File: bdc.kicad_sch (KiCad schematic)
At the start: 0 parts

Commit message: corrected output/input type of pins
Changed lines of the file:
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@@
 	)
 	(hierarchical_label "9"
-		(shape input)
+		(shape output)
 		(at 215.9 54.61 0)
 		(effects
@@
 	)
 	(hierarchical_label "0"
-		(shape input)
+		(shape output)
 		(at 118.11 31.75 0)
 		(effects
@@
 	)
 	(hierarchical_label "7"
-		(shape input)
+		(shape output)
 		(at 124.46 165.1 0)
 		(effects
@@
 	)
 	(hierarchical_label "8"
-		(shape input)
+		(shape output)
 		(at 215.9 36.83 0)
 		(effects
@@
 	)
 	(hierarchical_label "2"
-		(shape input)
+		(shape output)
 		(at 125.73 69.85 0)
 		(effects
@@
 	)
 	(hierarchical_label "6"
-		(shape input)
+		(shape output)
 		(at 124.46 147.32 0)
 		(effects
@@
 	)
 	(hierarchical_label "4"
-		(shape input)
+		(shape output)
 		(at 124.46 111.76 0)
 		(effects
@@
 	)
 	(hierarchical_label "5"
-		(shape input)
+		(shape output)
 		(at 124.46 129.54 0)
 		(effects
@@
 	)
 	(hierarchical_label "3"
-		(shape input)
+		(shape output)
 		(at 125.73 87.63 0)
 		(effects
@@
 	)
 	(hierarchical_label "1"
-		(shape input)
+		(shape output)
 		(at 125.73 52.07 0)
 		(effects
@@
 			)
 		)
-		(pin "Out" input
+		(pin "Out" output
 			(at 176.53 38.1 0)
 			(effects
@@
 			)
 		)
-		(pin "Out" input
+		(pin "Out" output
 			(at 118.11 111.76 0)
 			(effects
@@
 			)
 		)
-		(pin "Out" input
+		(pin "Out" output
 			(at 86.36 31.75 0)
 			(effects
@@
 			)
 		)
-		(pin "Out" input
+		(pin "Out" output
 			(at 118.11 129.54 0)
 			(effects
@@
 			)
 		)
-		(pin "Out" input
+		(pin "Out" output
 			(at 119.38 69.85 0)
 			(effects
@@
 			)
 		)
-		(pin "Out" input
+		(pin "Out" output
 			(at 119.38 52.07 0)
 			(effects
@@
 			)
 		)
-		(pin "Out" input
+		(pin "Out" output
 			(at 119.38 87.63 0)
 			(effects
@@
 			)
 		)
-		(pin "Out" input
+		(pin "Out" output
 			(at 209.55 54.61 0)
 			(effects
@@
 			)
 		)
-		(pin "Out" input
+		(pin "Out" output
 			(at 209.55 36.83 0)
 			(effects
@@
 			)
 		)
-		(pin "Out" input
+		(pin "Out" output
 			(at 118.11 165.1 0)
 			(effects
@@
 			)
 		)
-		(pin "Out" input
+		(pin "Out" output
 			(at 86.36 57.15 0)
 			(effects
@@
 			)
 		)
-		(pin "Out" input
+		(pin "Out" output
 			(at 118.11 147.32 0)
 			(effects

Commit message: schematic cleanup, routed 1 bdc
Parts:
- added C50, C53, C56: 100n, Capacitor_SMD:C_0603_1608Metric, symbol Device:C
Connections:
- new net +3V3: C50.1, C53.1, C56.1
- new net GND: C50.2, C53.2, C56.2

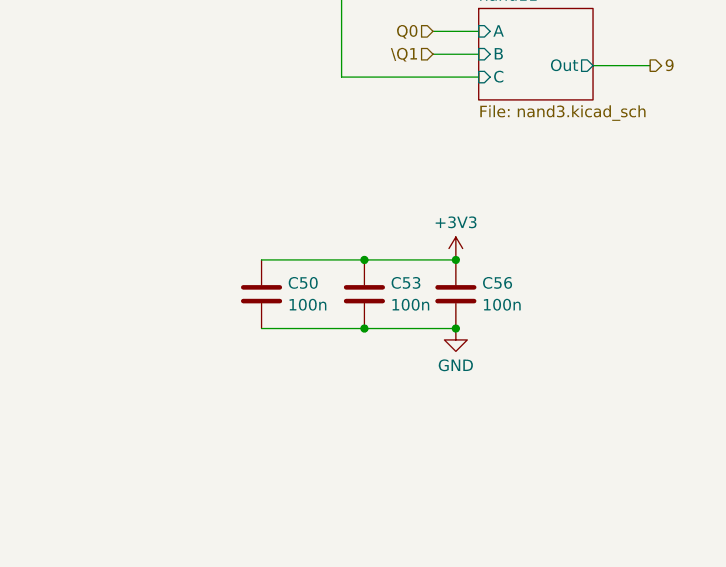
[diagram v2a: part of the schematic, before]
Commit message: started on binary to decimal converter
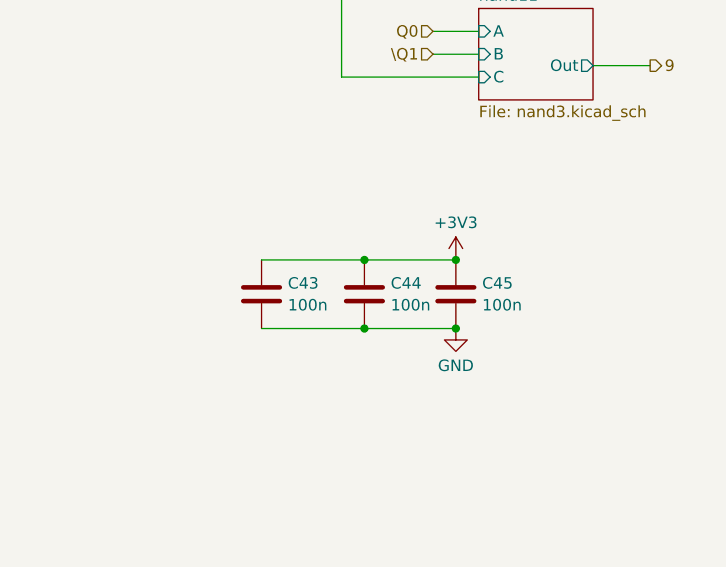
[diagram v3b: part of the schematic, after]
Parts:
- renumbered C50 to C43, C53 to C44, C56 to C45
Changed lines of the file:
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@@
 		(dnp no)
 		(fields_autoplaced yes)
-		(property "Reference" "C50"
+		(property "Reference" "C43"
 			(at 175.641 78.7978 0)
 			(effects
@@
 			(project "transistor-clock"
 				(path "/ce10d5bc-995e-4952-aa76-0a08f713a0f2/2c36a9e9-de42-4705-9ad4-94f4cc168e2f/49b62d3b-7090-4f14-b374-032413294413"
-					(reference "C52")
-					(unit 1)
-				)
-				(path "/ce10d5bc-995e-4952-aa76-0a08f713a0f2/2c36a9e9-de42-4705-9ad4-94f4cc168e2f/b52e17f4-8de5-4ac3-9a56-8e7fd7073d2b"
-					(reference "C50")
-					(unit 1)
-				)
-				(path "/ce10d5bc-995e-4952-aa76-0a08f713a0f2/2c36a9e9-de42-4705-9ad4-94f4cc168e2f/e3090ade-adf9-41e7-9c4d-7ceb9518aa28"
-					(reference "C51")
+					(reference "C49")
+					(unit 1)
+				)
+				(path "/ce10d5bc-995e-4952-aa76-0a08f713a0f2/2c36a9e9-de42-4705-9ad4-94f4cc168e2f/b52e17f4-8de5-4ac3-9a56-8e7fd7073d2b"
+					(reference "C43")
+					(unit 1)
+				)
+				(path "/ce10d5bc-995e-4952-aa76-0a08f713a0f2/2c36a9e9-de42-4705-9ad4-94f4cc168e2f/e3090ade-adf9-41e7-9c4d-7ceb9518aa28"
+					(reference "C46")
 					(unit 1)
 				)
@@
 		(dnp no)
 		(fields_autoplaced yes)
-		(property "Reference" "C56"
+		(property "Reference" "C45"
 			(at 197.231 78.7978 0)
 			(effects
@@
 			(project "transistor-clock"
 				(path "/ce10d5bc-995e-4952-aa76-0a08f713a0f2/2c36a9e9-de42-4705-9ad4-94f4cc168e2f/49b62d3b-7090-4f14-b374-032413294413"
-					(reference "C58")
-					(unit 1)
-				)
-				(path "/ce10d5bc-995e-4952-aa76-0a08f713a0f2/2c36a9e9-de42-4705-9ad4-94f4cc168e2f/b52e17f4-8de5-4ac3-9a56-8e7fd7073d2b"
-					(reference "C56")
-					(unit 1)
-				)
-				(path "/ce10d5bc-995e-4952-aa76-0a08f713a0f2/2c36a9e9-de42-4705-9ad4-94f4cc168e2f/e3090ade-adf9-41e7-9c4d-7ceb9518aa28"
-					(reference "C57")
+					(reference "C51")
+					(unit 1)
+				)
+				(path "/ce10d5bc-995e-4952-aa76-0a08f713a0f2/2c36a9e9-de42-4705-9ad4-94f4cc168e2f/b52e17f4-8de5-4ac3-9a56-8e7fd7073d2b"
+					(reference "C45")
+					(unit 1)
+				)
+				(path "/ce10d5bc-995e-4952-aa76-0a08f713a0f2/2c36a9e9-de42-4705-9ad4-94f4cc168e2f/e3090ade-adf9-41e7-9c4d-7ceb9518aa28"
+					(reference "C48")
 					(unit 1)
 				)
@@
 		(dnp no)
 		(fields_autoplaced yes)
-		(property "Reference" "#PWR0384"
+		(property "Reference" "#PWR0256"
 			(at 194.31 80.01 0)
 			(effects
@@
 			(project "transistor-clock"
 				(path "/ce10d5bc-995e-4952-aa76-0a08f713a0f2/2c36a9e9-de42-4705-9ad4-94f4cc168e2f/49b62d3b-7090-4f14-b374-032413294413"
-					(reference "#PWR0388")
-					(unit 1)
-				)
-				(path "/ce10d5bc-995e-4952-aa76-0a08f713a0f2/2c36a9e9-de42-4705-9ad4-94f4cc168e2f/b52e17f4-8de5-4ac3-9a56-8e7fd7073d2b"
-					(reference "#PWR0384")
-					(unit 1)
-				)
-				(path "/ce10d5bc-995e-4952-aa76-0a08f713a0f2/2c36a9e9-de42-4705-9ad4-94f4cc168e2f/e3090ade-adf9-41e7-9c4d-7ceb9518aa28"
-					(reference "#PWR0386")
+					(reference "#PWR0324")
+					(unit 1)
+				)
+				(path "/ce10d5bc-995e-4952-aa76-0a08f713a0f2/2c36a9e9-de42-4705-9ad4-94f4cc168e2f/b52e17f4-8de5-4ac3-9a56-8e7fd7073d2b"
+					(reference "#PWR0256")
+					(unit 1)
+				)
+				(path "/ce10d5bc-995e-4952-aa76-0a08f713a0f2/2c36a9e9-de42-4705-9ad4-94f4cc168e2f/e3090ade-adf9-41e7-9c4d-7ceb9518aa28"
+					(reference "#PWR0296")
 					(unit 1)
 				)
@@
 		(dnp no)
 		(fields_autoplaced yes)
-		(property "Reference" "C53"
+		(property "Reference" "C44"
 			(at 187.071 78.7978 0)
 			(effects
@@
 			(project "transistor-clock"
 				(path "/ce10d5bc-995e-4952-aa76-0a08f713a0f2/2c36a9e9-de42-4705-9ad4-94f4cc168e2f/49b62d3b-7090-4f14-b374-032413294413"
-					(reference "C55")
-					(unit 1)
-				)
-				(path "/ce10d5bc-995e-4952-aa76-0a08f713a0f2/2c36a9e9-de42-4705-9ad4-94f4cc168e2f/b52e17f4-8de5-4ac3-9a56-8e7fd7073d2b"
-					(reference "C53")
-					(unit 1)
-				)
-				(path "/ce10d5bc-995e-4952-aa76-0a08f713a0f2/2c36a9e9-de42-4705-9ad4-94f4cc168e2f/e3090ade-adf9-41e7-9c4d-7ceb9518aa28"
-					(reference "C54")
+					(reference "C50")
+					(unit 1)
+				)
+				(path "/ce10d5bc-995e-4952-aa76-0a08f713a0f2/2c36a9e9-de42-4705-9ad4-94f4cc168e2f/b52e17f4-8de5-4ac3-9a56-8e7fd7073d2b"
+					(reference "C44")
+					(unit 1)
+				)
+				(path "/ce10d5bc-995e-4952-aa76-0a08f713a0f2/2c36a9e9-de42-4705-9ad4-94f4cc168e2f/e3090ade-adf9-41e7-9c4d-7ceb9518aa28"
+					(reference "C47")
 					(unit 1)
 				)
@@
 		(dnp no)
 		(fields_autoplaced yes)
-		(property "Reference" "#PWR0385"
+		(property "Reference" "#PWR0257"
 			(at 194.31 90.17 0)
 			(effects
@@
 			(project "transistor-clock"
 				(path "/ce10d5bc-995e-4952-aa76-0a08f713a0f2/2c36a9e9-de42-4705-9ad4-94f4cc168e2f/49b62d3b-7090-4f14-b374-032413294413"
-					(reference "#PWR0389")
-					(unit 1)
-				)
-				(path "/ce10d5bc-995e-4952-aa76-0a08f713a0f2/2c36a9e9-de42-4705-9ad4-94f4cc168e2f/b52e17f4-8de5-4ac3-9a56-8e7fd7073d2b"
-					(reference "#PWR0385")
-					(unit 1)
-				)
-				(path "/ce10d5bc-995e-4952-aa76-0a08f713a0f2/2c36a9e9-de42-4705-9ad4-94f4cc168e2f/e3090ade-adf9-41e7-9c4d-7ceb9518aa28"
-					(reference "#PWR0387")
-					(unit 1)
-				)
+					(reference "#PWR0325")
+					(unit 1)
+				)
+				(path "/ce10d5bc-995e-4952-aa76-0a08f713a0f2/2c36a9e9-de42-4705-9ad4-94f4cc168e2f/b52e17f4-8de5-4ac3-9a56-8e7fd7073d2b"
+					(reference "#PWR0257")
+					(unit 1)
+				)
+				(path "/ce10d5bc-995e-4952-aa76-0a08f713a0f2/2c36a9e9-de42-4705-9ad4-94f4cc168e2f/e3090ade-adf9-41e7-9c4d-7ceb9518aa28"
+					(reference "#PWR0297")
+					(unit 1)
+				)

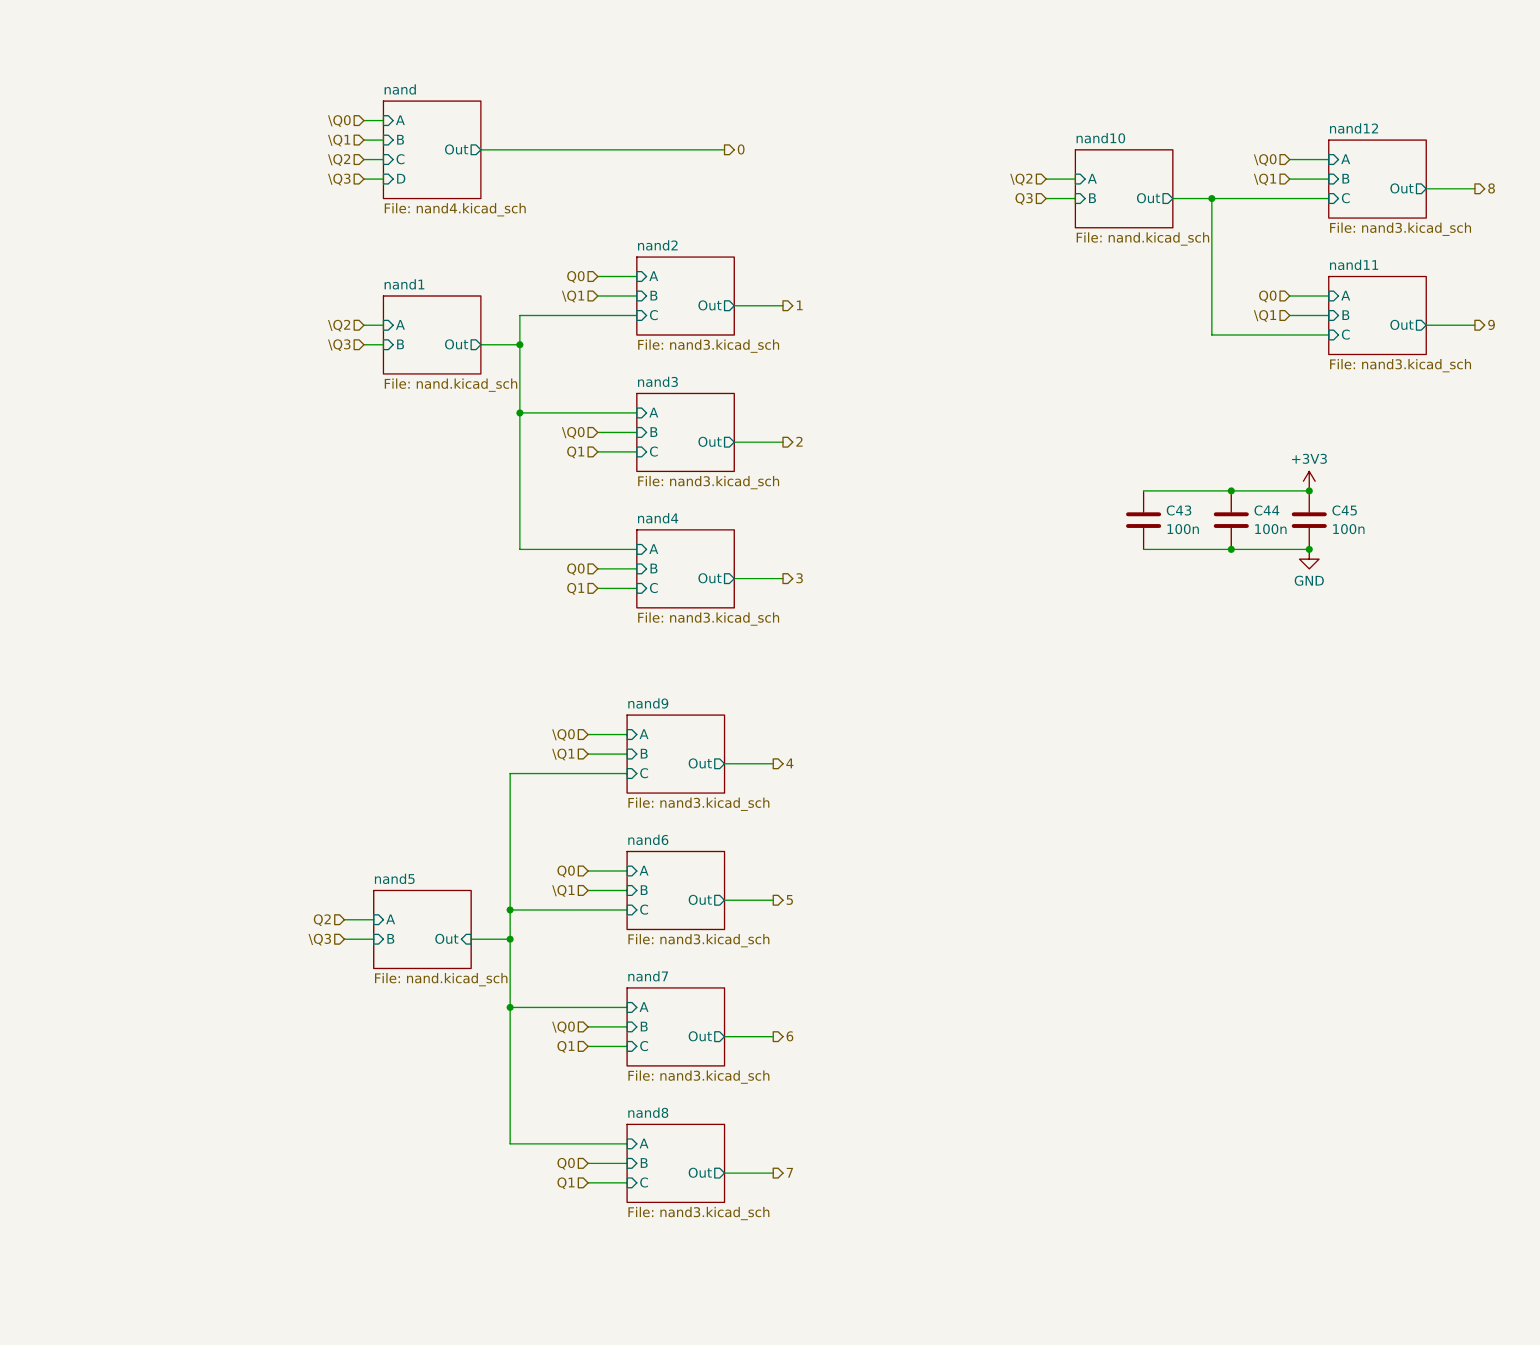
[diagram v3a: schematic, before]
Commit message: replace bcd logic with bin-to-dec module
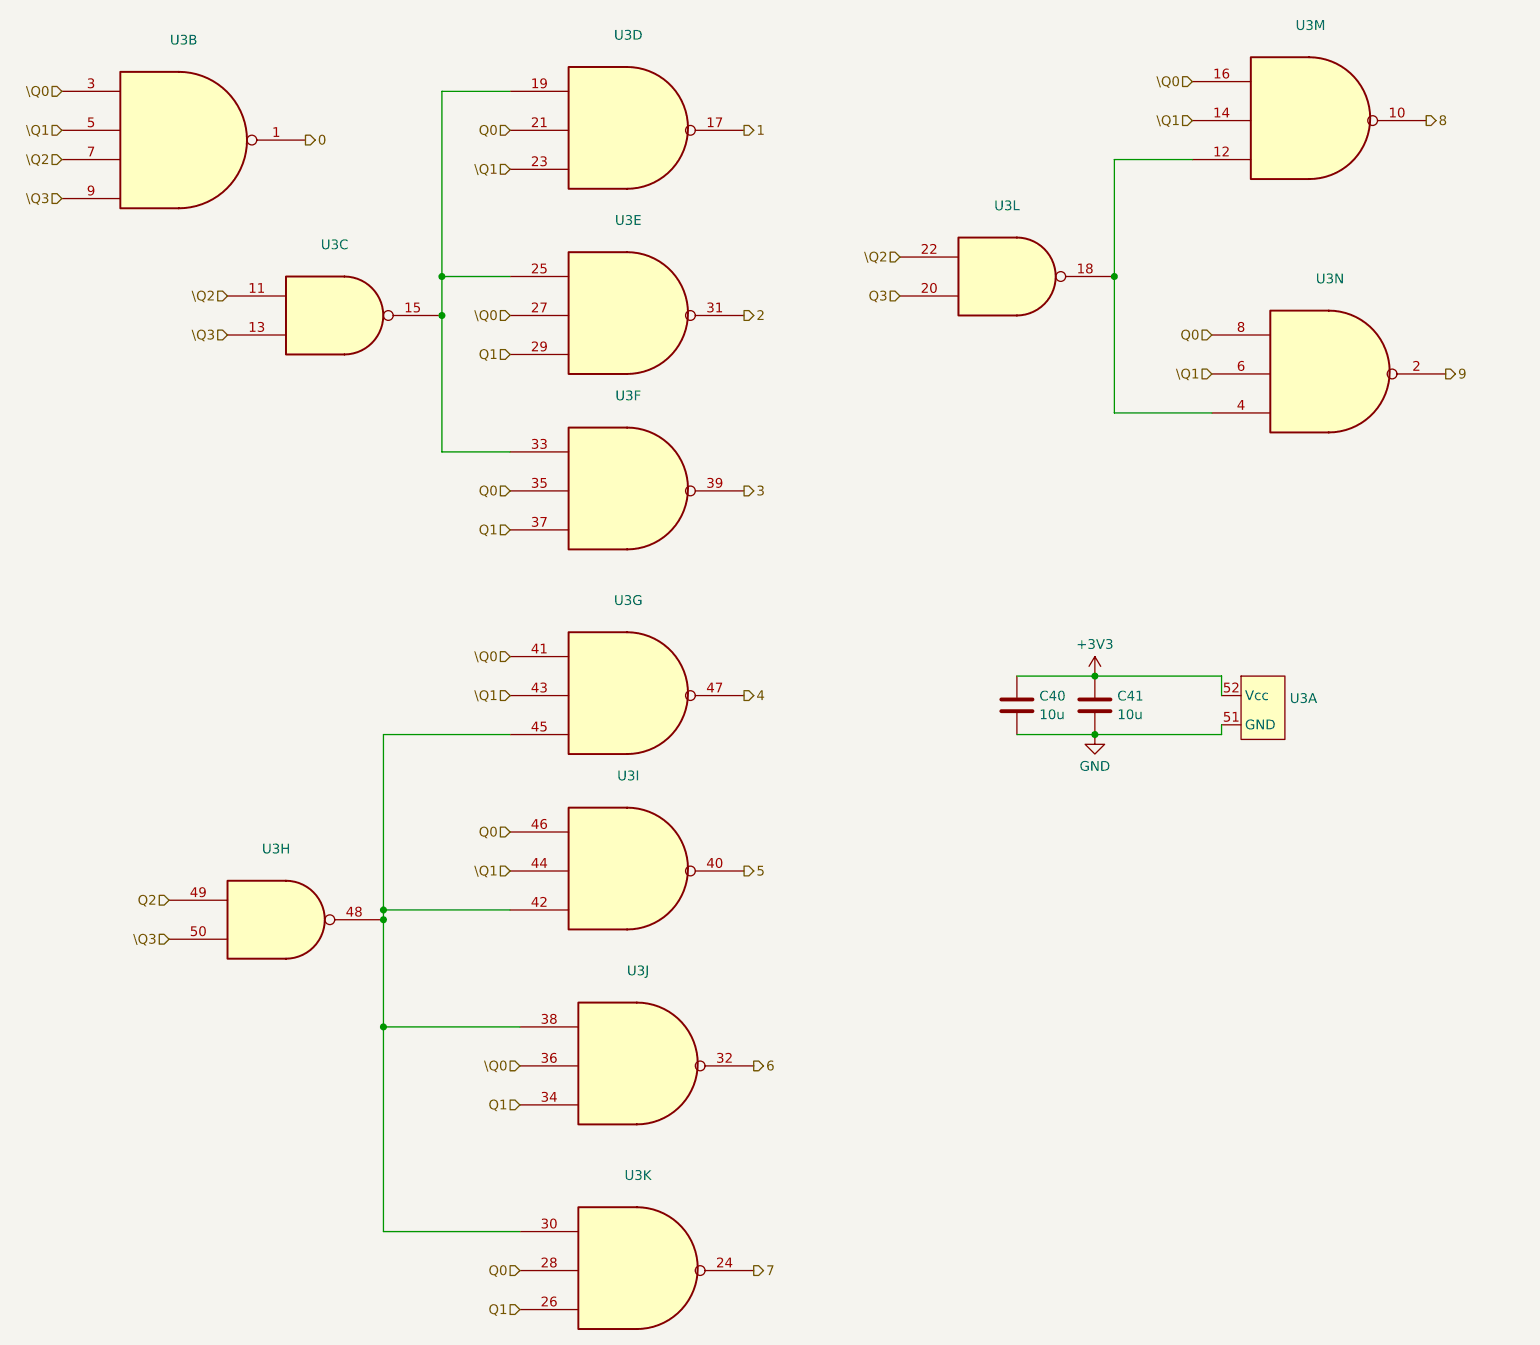
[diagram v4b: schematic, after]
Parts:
- removed C43: 100n, Capacitor_SMD:C_0603_1608Metric, symbol Device:C
- added U3: ~, symbol custom:BDC_nands
- C40: renamed from C44; value 100n -> 10u
- C41: renamed from C45; value 100n -> 10u
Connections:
- net +3V3: now also U3.52 (Vcc)
- net 0: now also U3.1
- net 1: now also U3.17
- net 2: now also U3.31
- net 3: now also U3.39
- net 4: now also U3.47
- net 5: now also U3.40
- net 6: now also U3.32
- net 7: now also U3.24
- net 8: now also U3.10
- net 9: now also U3.2
- net GND: now also U3.51 (GND)
- net Q0: now also U3.21, U3.28, U3.35, U3.46, U3.8
- net Q1: now also U3.26, U3.29, U3.34, U3.37
- net Q2: now also U3.49
- net Q3: now also U3.20
- net \Q0: now also U3.16, U3.27, U3.3, U3.36, U3.41
- net \Q1: now also U3.14, U3.23, U3.43, U3.44, U3.5, U3.6
- net \Q2: now also U3.11, U3.22, U3.7
- net \Q3: now also U3.13, U3.50, U3.9
- new net: U3.12, U3.18, U3.4
- new net: U3.30, U3.38, U3.42, U3.45, U3.48
- new net: U3.15, U3.19, U3.25, U3.33
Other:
- removed sheet nand
- removed sheet nand1
- removed sheet nand10
- removed sheet nand11
- removed sheet nand12
- removed sheet nand2
- removed sheet nand3
- removed sheet nand4
- removed sheet nand5
- removed sheet nand6
- removed sheet nand7
- removed sheet nand8
- removed sheet nand9
- moved on the sheet: C40, C41

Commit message: added LCSC part numbers
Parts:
- C40, C41: LCSC Part # (none) -> C57112
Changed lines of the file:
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@@
+			)
+		)
+		(property "LCSC Part #" ""
+			(at 139.7 41.91 0)
+			(effects
+				(font
+					(size 1.27 1.27)
+				)
+				(hide yes)
 			)
 		)
@@
 			)
 		)
+		(property "LCSC Part #" ""
+			(at 88.9 142.24 0)
+			(effects
+				(font
+					(size 1.27 1.27)
+				)
+				(hide yes)
+			)
+		)
 		(pin "8"
 		)
@@
 			)
 		)
+		(property "LCSC Part #" ""
+			(at 88.9 67.31 0)
+			(effects
+				(font
+					(size 1.27 1.27)
+				)
+				(hide yes)
+			)
+		)
 		(pin "8"
 		)
@@
 			)
 		)
+		(property "LCSC Part #" ""
+			(at 175.26 16.51 0)
+			(effects
+				(font
+					(size 1.27 1.27)
+				)
+				(hide yes)
+			)
+		)
 		(pin "8"
 		)
@@
 			)
 		)
+		(property "LCSC Part #" ""
+			(at 38.1 21.59 0)
+			(effects
+				(font
+					(size 1.27 1.27)
+				)
+				(hide yes)
+			)
+		)
 		(pin "8"
 		)
@@
 			)
 		)
+		(property "LCSC Part #" "C57112"
+			(at 166.37 104.14 0)
+			(effects
+				(font
+					(size 1.27 1.27)
+				)
+				(hide yes)
+			)
+		)
 		(pin "2"
 		)
@@
 			)
 		)
+		(property "LCSC Part #" ""
+			(at 179.07 104.14 0)
+			(effects
+				(font
+					(size 1.27 1.27)
+				)
+				(hide yes)
+			)
+		)
 		(pin "8"
 		)
@@
 			)
 		)
+		(property "LCSC Part #" ""
+			(at 176.53 49.53 0)
+			(effects
+				(font
+					(size 1.27 1.27)
+				)
+				(hide yes)
+			)
+		)
 		(pin "8"
 		)
@@
 			)
 		)
+		(property "LCSC Part #" ""
+			(at 88.9 116.84 0)
+			(effects
+				(font
+					(size 1.27 1.27)
+				)
+				(hide yes)
+			)
+		)
 		(pin "8"
 		)
@@
 			)
 		)
+		(property "LCSC Part #" ""
+			(at 88.9 44.45 0)
+			(effects
+				(font
+					(size 1.27 1.27)
+				)
+				(hide yes)
+			)
+		)
 		(pin "8"
 		)
@@
 			)
 		)
+		(property "LCSC Part #" ""
+			(at 54.61 46.99 0)
+			(effects
+				(font
+					(size 1.27 1.27)
+				)
+				(hide yes)
+			)
+		)
 		(pin "8"
 		)
@@
 			)
 		)
+		(property "LCSC Part #" ""
+			(at 87.63 167.64 0)
+			(effects
+				(font
+					(size 1.27 1.27)
+				)
+				(hide yes)
+			)
+		)
 		(pin "8"
 		)
@@
 			)
 		)
+		(property "LCSC Part #" ""
+			(at 44.45 125.73 0)
+			(effects
+				(font
+					(size 1.27 1.27)
+				)
+				(hide yes)
+			)
+		)
 		(pin "8"
 		)
@@
 			)
 		)
+		(property "LCSC Part #" "C57112"
+			(at 156.21 104.14 0)
+			(effects
+				(font
+					(size 1.27 1.27)
+				)
+				(hide yes)
+			)
+		)
 		(pin "2"
 		)
@@
 			)
 		)
+		(property "LCSC Part #" ""
+			(at 90.17 20.32 0)
+			(effects
+				(font
+					(size 1.27 1.27)
+				)
+				(hide yes)
+			)
+		)
 		(pin "8"
 		)
@@
 			(at 90.17 93.98 0)
 			(effects
+				(font
+					(size 1.27 1.27)
+				)
+				(hide yes)
+			)
+		)
+		(property "LCSC Part #" ""
+			(at 90.17 93.98 0)
+			(effects
